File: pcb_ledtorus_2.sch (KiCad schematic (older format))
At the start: 16 parts, among them P1 CONN_02X04, P2 CONN_6, P3 MICRO-SD, P6 CONN_12, U1 STM32F46X_LQFP176, U2 US4881_HALL

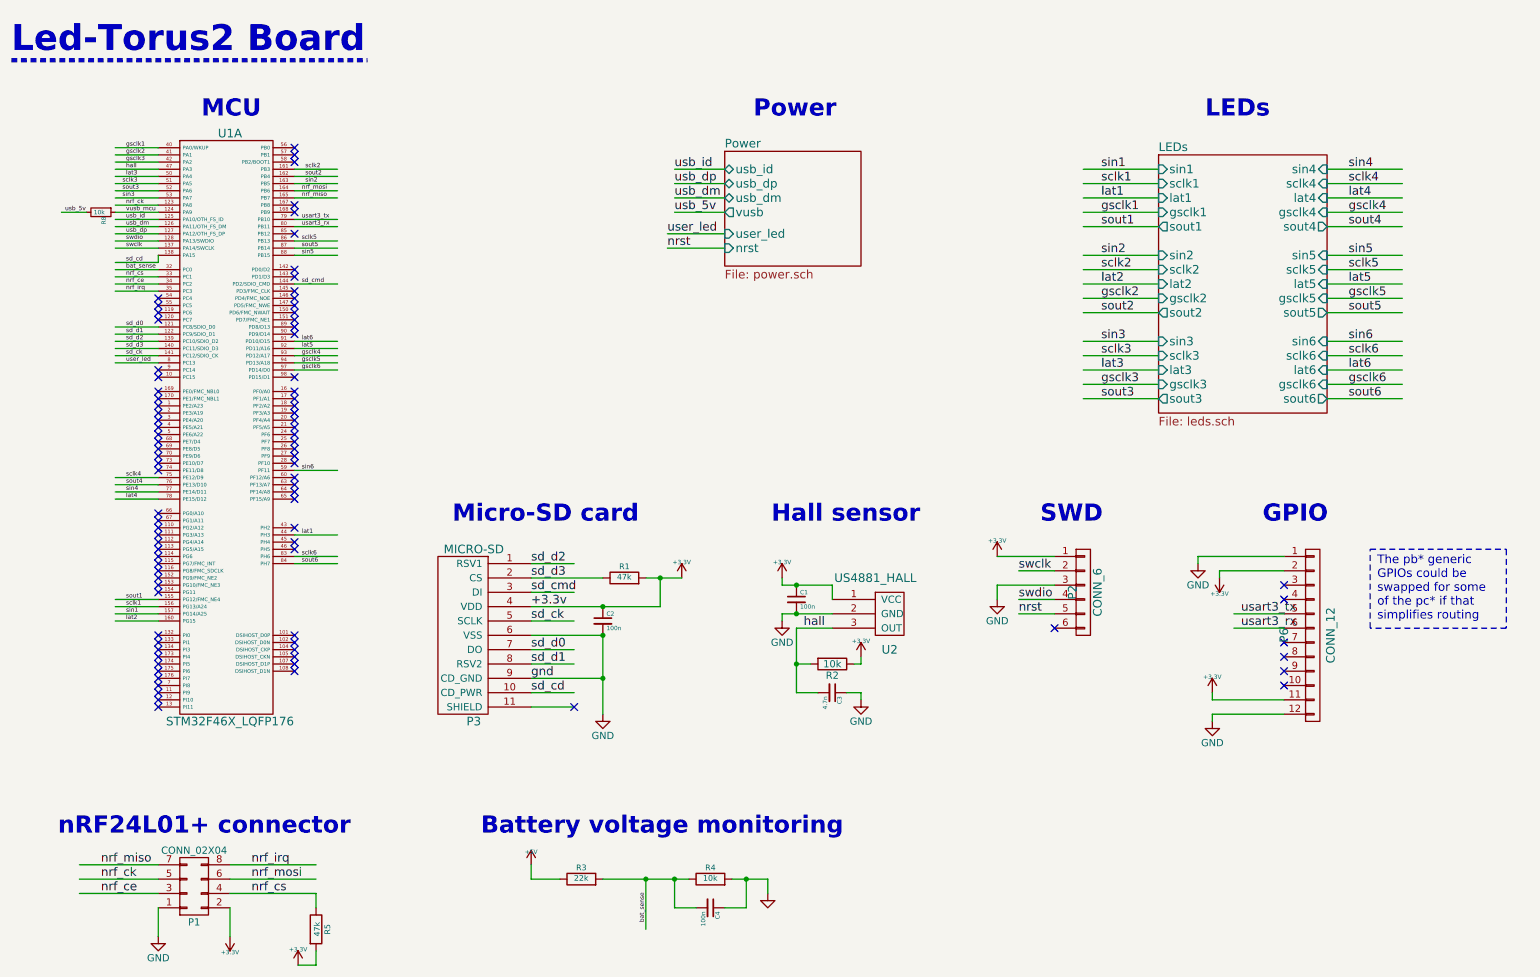
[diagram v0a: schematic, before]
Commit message: First version that fully passes DRC.
Still some polishing to do (like extra GPIO header, general cleanup, ...).
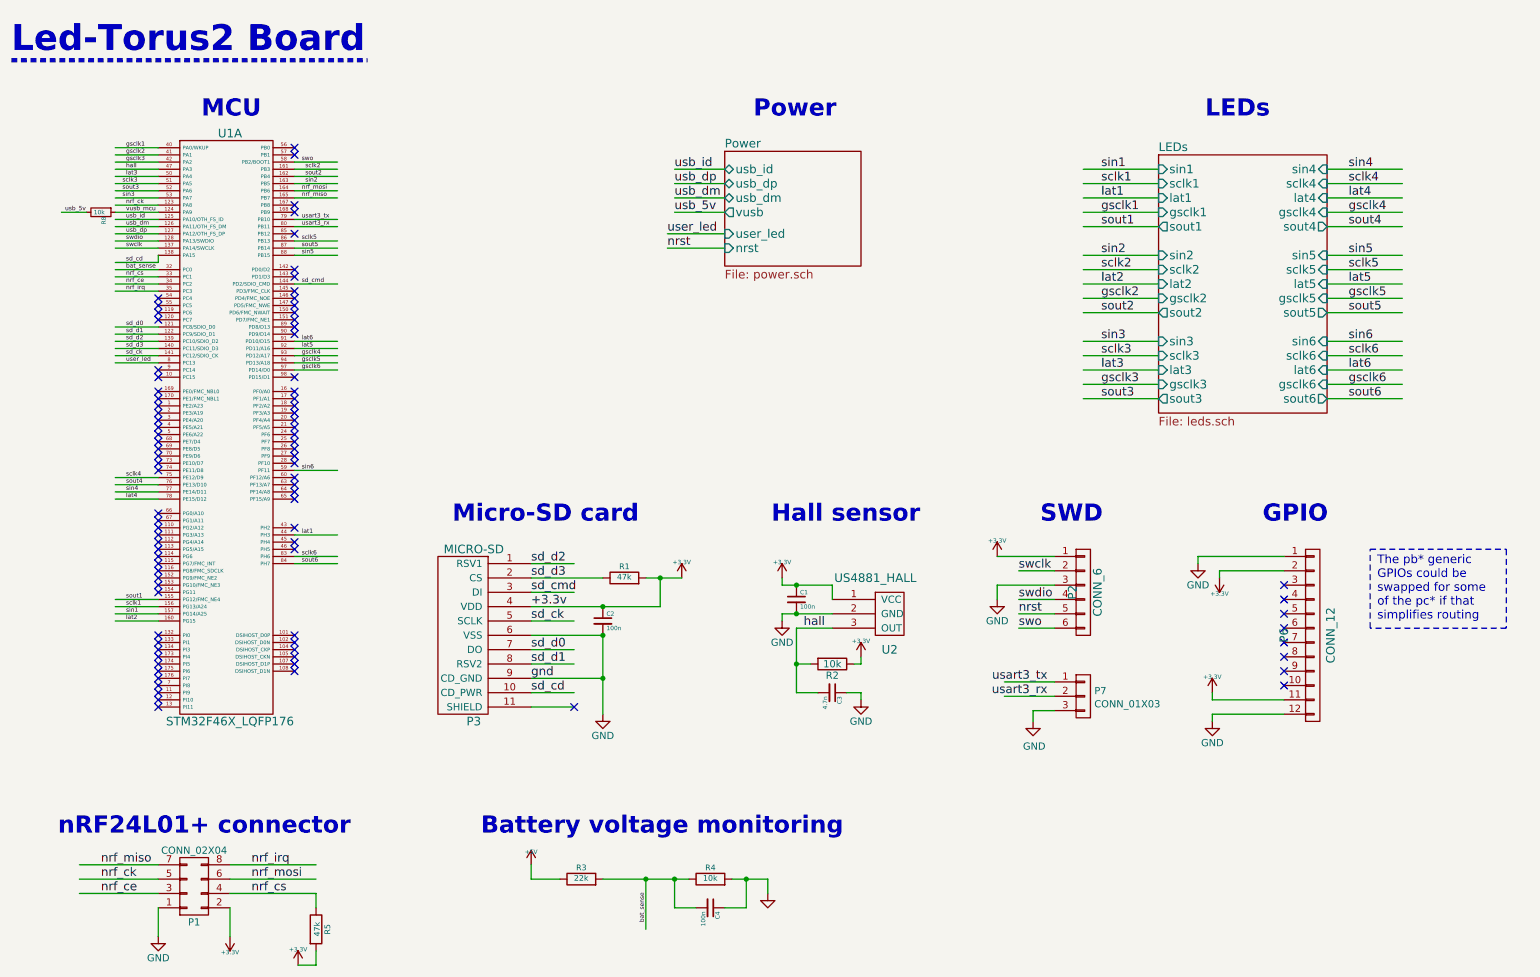
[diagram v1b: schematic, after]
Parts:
- added P7: CONN_01X03, Pin_Headers:Pin_Header_Straight_1x03, symbol CONN_01X03
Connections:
- net labels added: swo
- wire segments 156 -> 160
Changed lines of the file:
@@
 Text Label 7650 4600 0    60   ~ 0
 swdio
-NoConn ~ 7900 4800
 Text Label 7650 4700 0    60   ~ 0
 nrst
@@
 	1    0    0    -1
 $EndComp
-Text Label 9200 4700 0    60   ~ 0
-usart3_tx
-Text Label 9200 4800 0    60   ~ 0
-usart3_rx
 $Comp
 L +3.3V #PWR08
@@
 Wire Wire Line
 	8900 4300 9500 4300
-Wire Wire Line
-	9500 4700 9150 4700
-Wire Wire Line
-	9150 4800 9500 4800
 Wire Wire Line
 	9000 5300 9500 5300
@@
 Text Label 1425 1650 0    30   ~ 0
 lat3
-NoConn ~ 2600 1550
 NoConn ~ 2600 2050
 Wire Wire Line
@@
 Text Label 1000 1900 0    30   ~ 0
 usb_5v
+Text Label 7850 5175 2    60   ~ 0
+usart3_tx
+Text Label 7850 5275 2    60   ~ 0
+usart3_rx
+Wire Wire Line
+	7550 5175 7900 5175
+Wire Wire Line
+	7900 5275 7550 5275
+$Comp
+L CONN_01X03 P7
+U 1 1 56F289B7
+P 8100 5275
+F 0 "P7" H 8177 5313 50  0000 L CNN
+F 1 "CONN_01X03" H 8177 5221 50  0000 L CNN
+F 2 "Pin_Headers:Pin_Header_Straight_1x03" H 8100 5275 50  0001 C CNN
+F 3 "" H 8100 5275 50  0000 C CNN
+	1    8100 5275
+	1    0    0    -1
+$EndComp
+Wire Wire Line
+	7900 5375 7750 5375
+Wire Wire Line
+	7750 5375 7750 5450
+$Comp
+L GND #PWR018
+U 1 1 56F28DDB
+P 7750 5450
+F 0 "#PWR018" H 7750 5200 50  0001 C CNN
+F 1 "GND" H 7758 5276 50  0000 C CNN
+F 2 "" H 7750 5450 50  0000 C CNN
+F 3 "" H 7750 5450 50  0000 C CNN
+	1    7750 5450
+	1    0    0    -1
+$EndComp
+Wire Wire Line
+	2600 1550 2900 1550
+Text Label 2650 1550 0    30   ~ 0
+swo
+Wire Wire Line
+	7900 4800 7650 4800
+Text Label 7650 4800 0    60   ~ 0
+swo
+NoConn ~ 9500 4700
+NoConn ~ 9500 4800
 $EndSCHEMATC

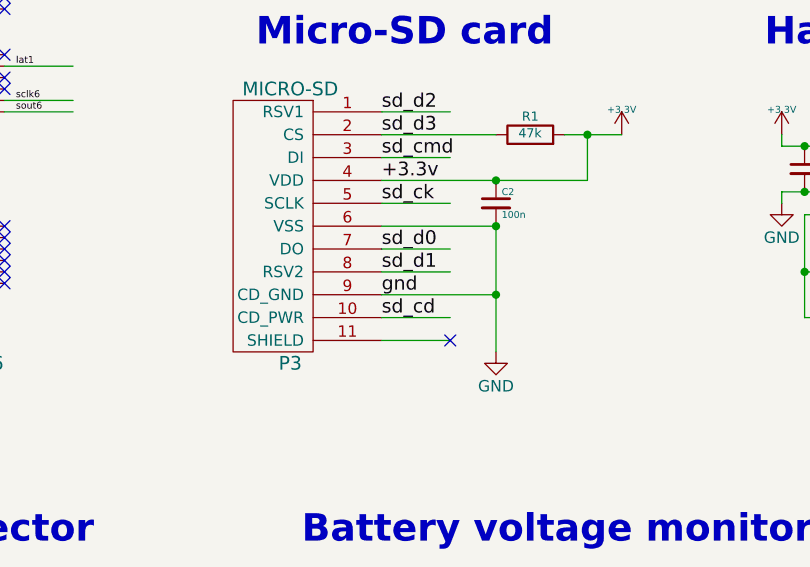
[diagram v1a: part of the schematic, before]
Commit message: Cleanup back routing on U7
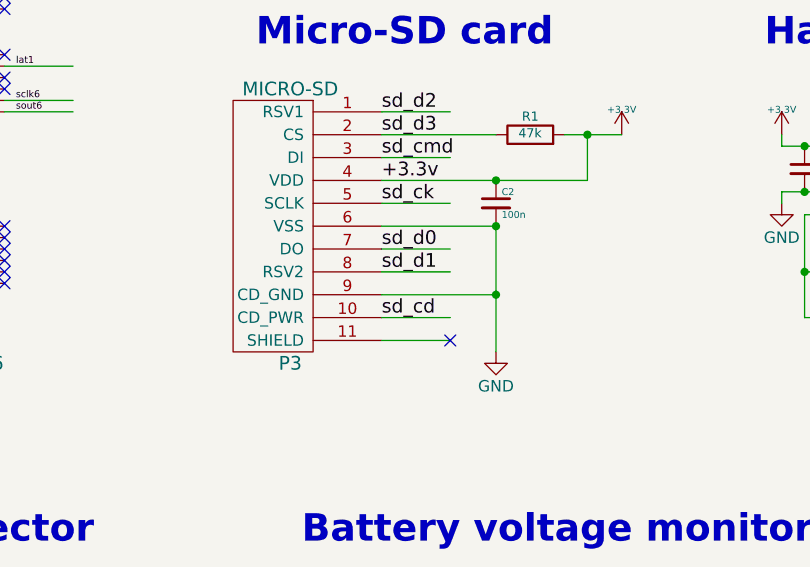
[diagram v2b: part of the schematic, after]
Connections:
- net labels removed: gnd
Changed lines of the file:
@@
 Text Label 4250 5250 0    60   ~ 0
 sd_cd
-Text Label 4250 5150 0    60   ~ 0
-gnd
 Text Label 4250 4950 0    60   ~ 0
 sd_d0

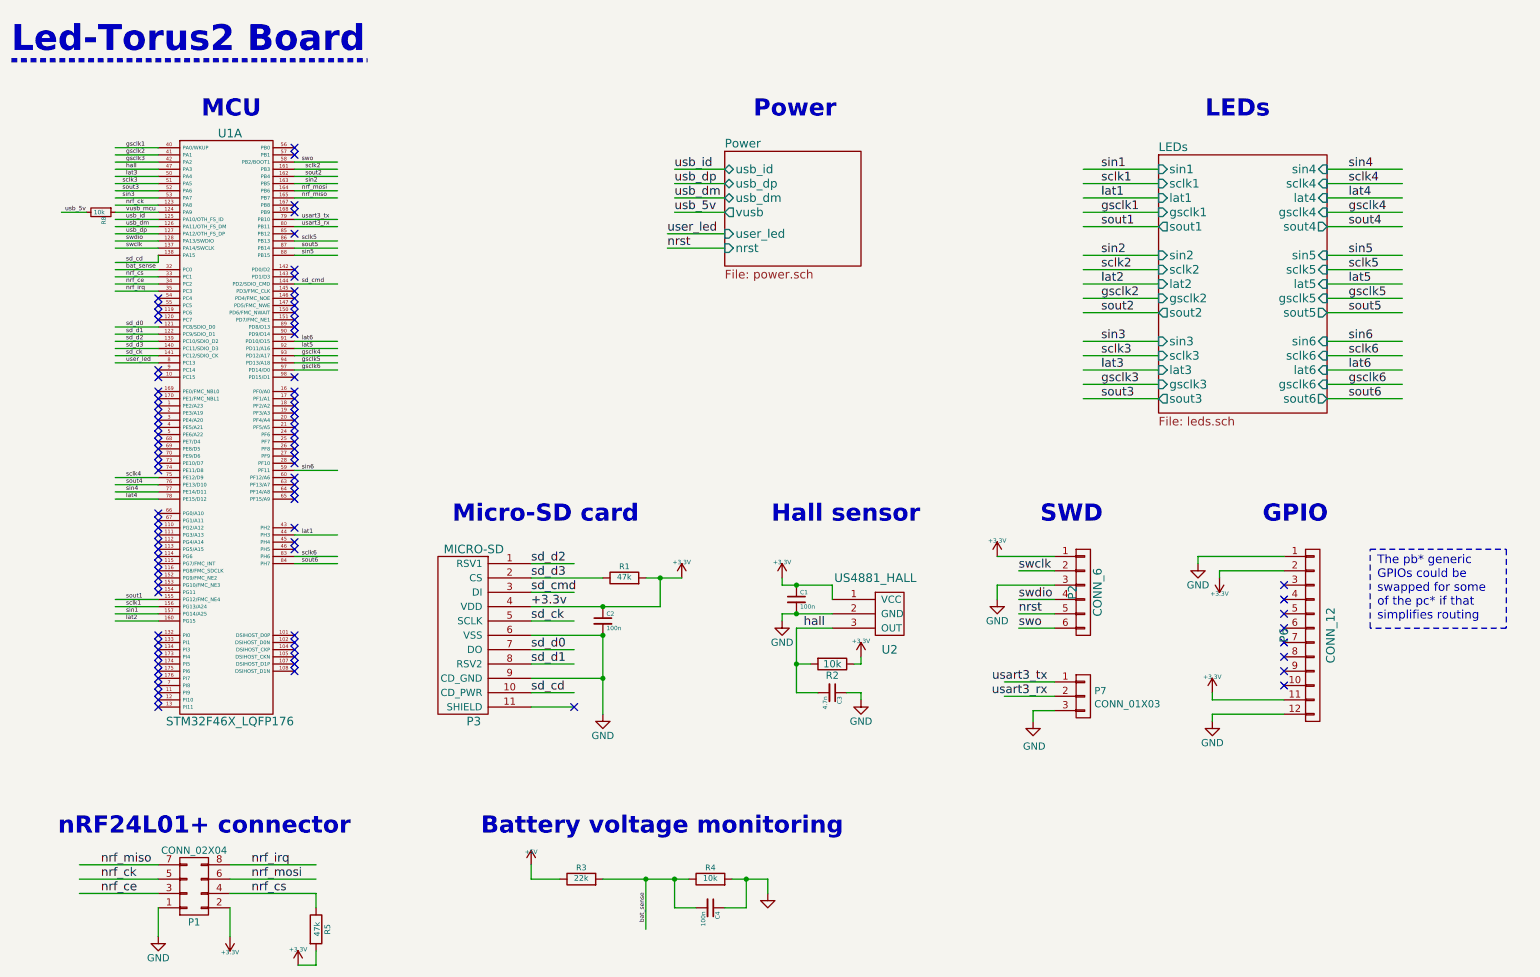
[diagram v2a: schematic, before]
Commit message: Create new GPIO header.
Has 14 GPIOs with reasonable availability of peripherals (timers, usarts, ...).

The location is in upper left; USB is moved to the middle left.

(Neither USB nor generic GPIO are expected to be populated on the
actual LED-torus, but could turn out useful for other purposes).

Routing for this is preliminary, needs cleanup.
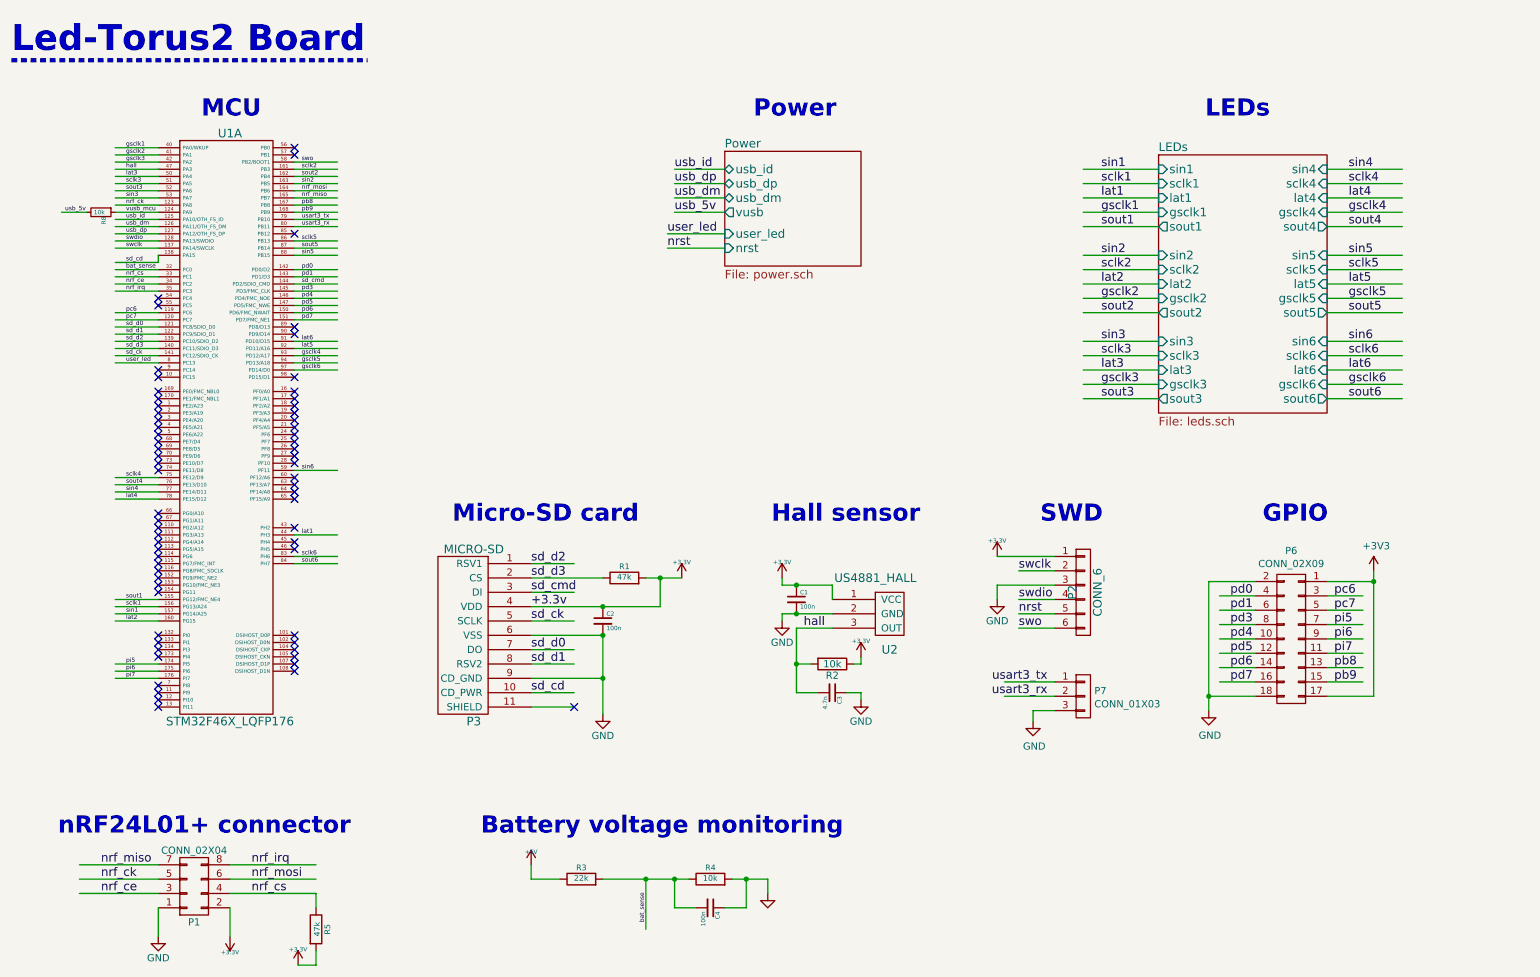
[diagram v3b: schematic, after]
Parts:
- removed P6: CONN_12, w_pin_strip:pin_strip_12-90, symbol CONN_01X12
- added P6: CONN_02X09, Pin_Headers:Pin_Header_Straight_2x09, symbol CONN_02X09
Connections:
- net labels added: +3V3, pb8, pb9, pc6, pc7, pd0, pd1, pd3, pd4, pd5, pd6, pd7, pi5, pi6, pi7
- wire segments 160 -> 186
- no-connect marks 89 -> 67
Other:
- note removed: "The pb* generic\nGPIOs could be\nswapped for some\nof the pc* if that\nsimplifies routing"

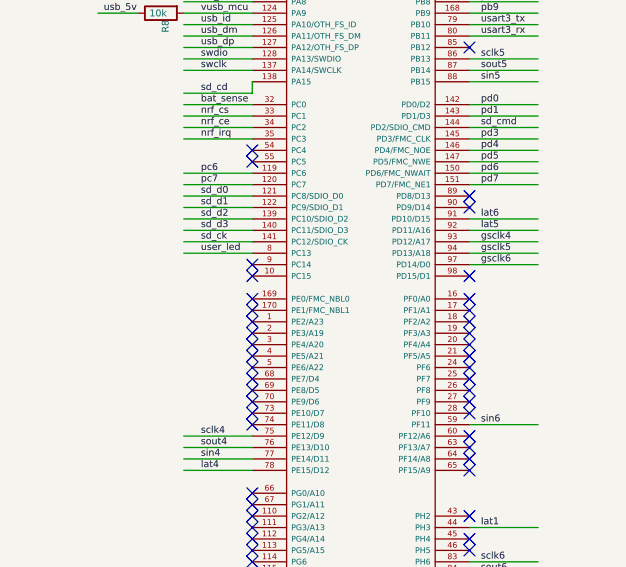
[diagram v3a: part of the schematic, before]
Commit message: Switch user LED to PE2.
(PC13, as it was before, has limited current sink capabilities).
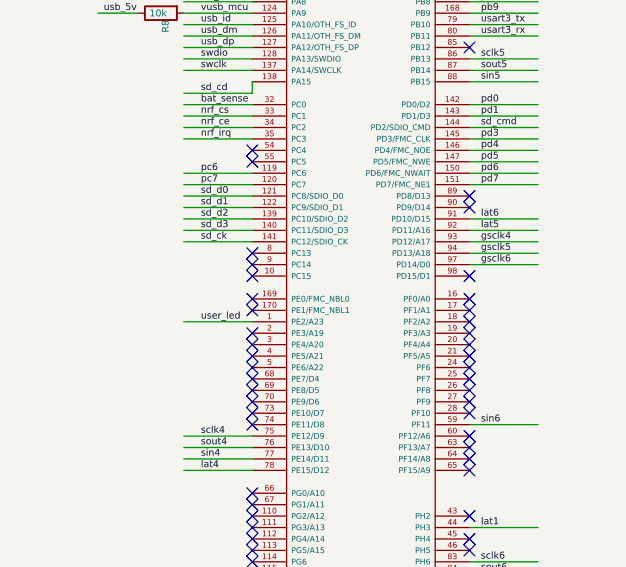
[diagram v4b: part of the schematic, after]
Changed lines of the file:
@@
 	1650 2900 1350 2900
 Wire Wire Line
-	1650 2950 1350 2950
+	1650 3250 1350 3250
 Wire Wire Line
 	1650 2200 1650 2250
@@
 Text Label 1425 4750 0    30   ~ 0
 lat2
-Text Label 1425 2950 0    30   ~ 0
+Text Label 1425 3250 0    30   ~ 0
 user_led
 Text Label 1425 2300 0    30   ~ 0
@@
 NoConn ~ 1650 3150
 NoConn ~ 1650 3200
-NoConn ~ 1650 3250
+NoConn ~ 1650 2950
 NoConn ~ 1650 3300
 NoConn ~ 1650 3350

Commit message: Remove incorrect routing of PB2 as SWO.
Also some misc. routing cleanups.
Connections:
- net labels removed: swo
- wire segments 186 -> 184
- no-connect marks 67 -> 69
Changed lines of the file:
@@
 	1    0    0    -1
 $EndComp
-Wire Wire Line
-	2600 1550 2900 1550
-Text Label 2650 1550 0    30   ~ 0
-swo
-Wire Wire Line
-	7900 4800 7650 4800
-Text Label 7650 4800 0    60   ~ 0
-swo
 $Comp
 L CONN_02X09 P6
@@
 Text Label 9850 5175 0    60   ~ 0
 pb9
+NoConn ~ 7900 4800
+NoConn ~ 2600 1550
 $EndSCHEMATC
